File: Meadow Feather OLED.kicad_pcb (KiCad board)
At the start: 2 copper layers, 23.4 x 74 mm, 15 parts, among them J1 Meadow_F7_Feather, J2 Conn_01x04

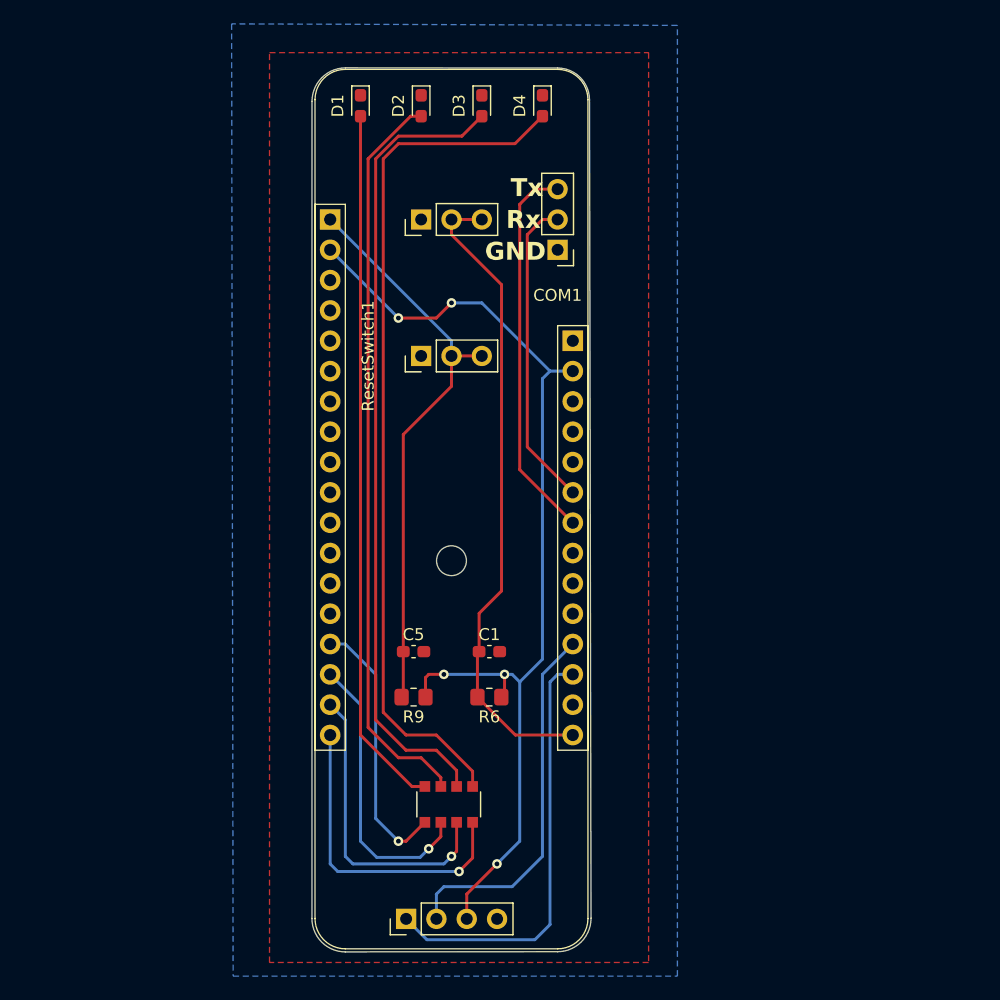
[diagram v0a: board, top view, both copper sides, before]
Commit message: Updated to V2.1 fixing: * Unconnected D3 and GND * Rounded tracks for the 1970s feel * Corrected LED resistor footprint
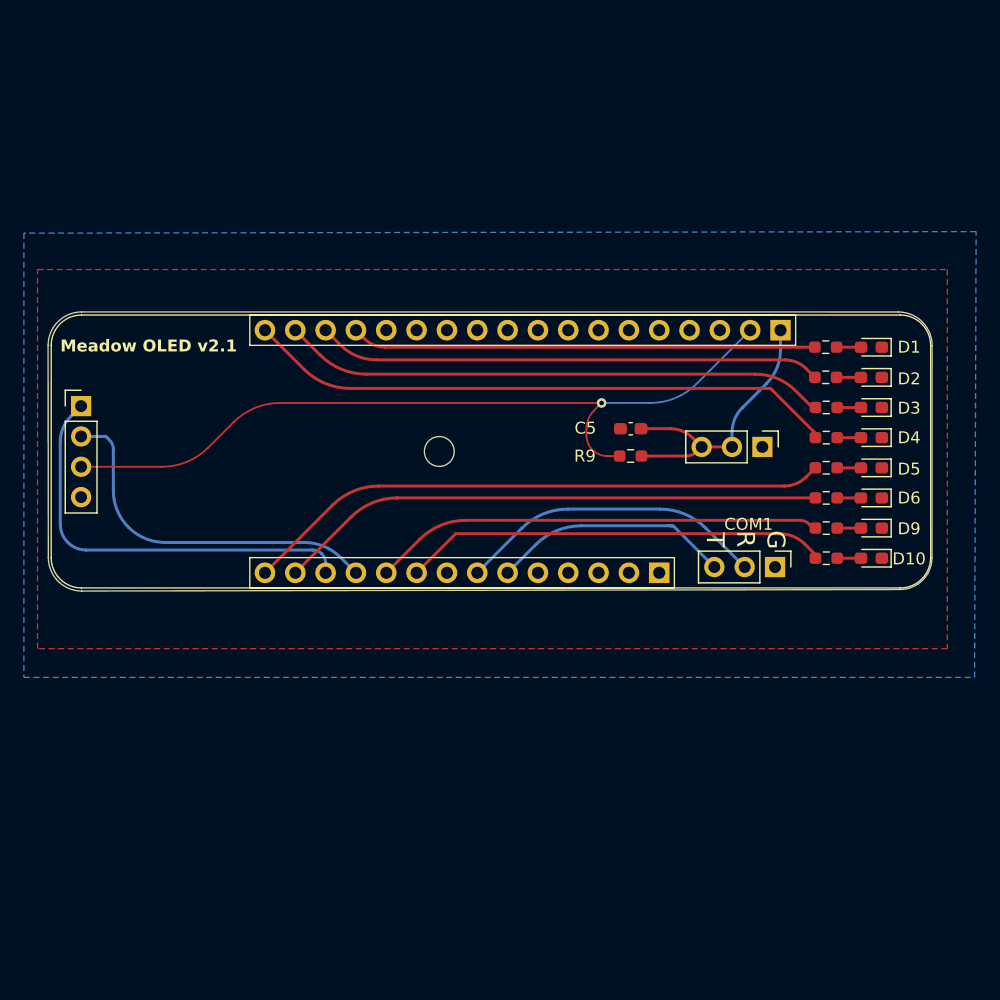
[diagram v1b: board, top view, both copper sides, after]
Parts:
- removed C1: C, Capacitor_SMD:C_0603_1608Metric_Pad1.08x0.95mm_HandSolder
- removed R6: R, Resistor_SMD:R_0805_2012Metric_Pad1.20x1.40mm_HandSolder
- removed RN1: R_Pack04, Resistor_SMD:R_Array_Convex_4x1206
- added D10: LED, LED_SMD:LED_0603_1608Metric_Pad1.05x0.95mm_HandSolder, F.Cu at (113.9, 86.8)
- added D6: LED, LED_SMD:LED_0603_1608Metric_Pad1.05x0.95mm_HandSolder, F.Cu at (113.9, 81.7)
- added D9: LED, LED_SMD:LED_0603_1608Metric_Pad1.05x0.95mm_HandSolder, F.Cu at (113.9, 84.3)
- added R1: R, Resistor_SMD:R_0603_1608Metric_Pad0.98x0.95mm_HandSolder, F.Cu at (110.1, 69.1)
- added R10: R, Resistor_SMD:R_0603_1608Metric_Pad0.98x0.95mm_HandSolder, F.Cu at (110.1, 86.8)
- added R2: R, Resistor_SMD:R_0603_1608Metric_Pad0.98x0.95mm_HandSolder, F.Cu at (110.1, 71.6)
- added R3: R, Resistor_SMD:R_0603_1608Metric_Pad0.98x0.95mm_HandSolder, F.Cu at (110.1, 74.2)
- added R4: R, Resistor_SMD:R_0603_1608Metric_Pad0.98x0.95mm_HandSolder, F.Cu at (110.1, 76.7)
- added R5: R, Resistor_SMD:R_0603_1608Metric_Pad0.98x0.95mm_HandSolder, F.Cu at (110.1, 79.2)
- added R7: R, Resistor_SMD:R_0603_1608Metric_Pad0.98x0.95mm_HandSolder, F.Cu at (110.1, 81.7)
- added R8: R, Resistor_SMD:R_0603_1608Metric_Pad0.98x0.95mm_HandSolder, F.Cu at (110.1, 84.3)
- D5: value SW_Push -> LED; footprint Connector_PinHeader_2.54mm:PinHeader_1x03_P2.54mm_Vertical -> LED_SMD:LED_0603_1608Metric_Pad1.05x0.95mm_HandSolder
- J1: footprint MCU_Wilderness_Labs:MeadowF7MicroFeatherOutline -> MCU_WildernessLabs:MeadowF7MicroFeatherOutline
- R9: footprint Resistor_SMD:R_0805_2012Metric_Pad1.20x1.40mm_HandSolder -> Resistor_SMD:R_0603_1608Metric_Pad0.98x0.95mm_HandSolder
- moved J2 50.8 mm to (47.7, 74.1), turned to 0 degrees
- moved D1 47.3 mm to (113.9, 69.1), turned to 180 degrees
- moved D2 44.0 mm to (113.9, 71.6), turned to 180 degrees
- moved D5 43.1 mm to (113.9, 79.2), turned to 180 degrees
- moved D3 41.3 mm to (113.9, 74.2), turned to 180 degrees
- moved D4 39.1 mm to (113.9, 76.7), turned to 180 degrees
- moved J1 38.8 mm to (106.3, 67.7), turned to -90 degrees
- moved COM1 32.2 mm to (105.8, 87.5), turned to -90 degrees
- moved ResetSwitch1 29.6 mm to (104.8, 77.5), turned to -90 degrees
- moved R9 27.2 mm to (93.7, 78.2), turned to 0 degrees
- moved C5 26.1 mm to (93.8, 75.9), turned to 180 degrees
- moved H5 9.21 mm to (77.7, 77.9), turned to -90 degrees
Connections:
- COM1 pad 2: /Rx -> /Tx
- COM1 pad 3: /Tx -> /Rx
- D5 pad 2: /D05 -> Net-(D5-A)
- J1 pad 25: unconnected-(J1-D11-Pad25) -> /D11
- J1 pad 31: /+3V3 -> unconnected-(J1-EN_+3V3-Pad31)
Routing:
- net Net-(D4-A): track 72.0 -> 2.14 mm
- net Net-(D3-A): track 67.2 -> 2.14 mm
- net Net-(D2-A): track 62.1 -> 2.14 mm
- net Net-(D1-A): track 59.0 -> 2.14 mm
- net /D06: track 0.00 -> 45.9 mm
- net /D09: track 0.00 -> 37.7 mm
- net /D10: track 0.00 -> 35.6 mm
- net /D04: track 26.4 -> 49.7 mm, vias 1 -> 0
- net /~Reset: track 48.5 -> 25.7 mm
- net /D03: track 25.7 -> 45.7 mm, vias 1 -> 0
- net /+3V3: track 86.3 -> 66.8 mm, vias 5 -> 1
- net /D02: track 24.2 -> 42.3 mm, vias 1 -> 0
- net /D01: track 22.5 -> 38.9 mm, vias 1 -> 0
- net /Rx: track 26.2 -> 20.1 mm
- net /Tx: track 32.2 -> 26.1 mm
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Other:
- board size 23.4 x 74 mm -> 74 x 23.4 mm
- board text added: "G"
- board text added: "Meadow OLED v2.1"
- board text added: "R"
- board text added: "T"
- board text removed: "GND"
- board text removed: "Rx"
- board text removed: "Tx"
